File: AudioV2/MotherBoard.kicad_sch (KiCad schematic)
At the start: 47 parts, among them J201 +15/-15/A_GND out, J202 PD module in (1=GND 2=+12V), SW402 PWR SW, SW501 DEST L (PHONE/MUTE/LINE), SW502 DEST R (PHONE/MUTE/LINE), U201 REC10K-2415DAW/H2, U202 L7809CV +9V, U402 PT2314E, U403 BP5293-50 +5V

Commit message: AudioV2: DC-DC を REC20K-2415DZ へ差し替え、電源要求を「ソケットあたり」で記録した
## なぜ

この箱はオペアンプを差し替えて聴く箱で、入力ブロードキャスト＋出力のみ MUX なので
10個が常時通電する。つまり +15V の要求は「NE5532 ×10」ではなく「挿す石 ×10、常時」で、
レールの余裕は**1ソケットあたり何 mA 使えるか**に翻訳しないと目的と噛み合わない。

Audio/datasheets/opamps/ の一次資料（在庫石の Icc）:
  MUSES03  20 mA/socket（10 mA max ×2 の変換基板）← 在庫の最悪
  NE5532   16 mA（ICC total、VO=0 無負荷。typ 6 mA）
  OPA627×2 15 mA / LT1364 15 mA / OPA1656 9.2 mA/pkg max

1ソケットあたりに使える電流（固定側を保守側の 63 mA として）:

              計測系そのまま  LDO を +15V へ  +5V_D も +15V へ
  REC10K       27.0 mA        19.0 mA         9.4 mA
  REC20K       60.4 mA        52.4 mA        42.8 mA

REC10K では計測系を触らなくても 27 mA/socket しか出ない。MUSES03(20mA) は通るが
ディスクリート DIP-8 モジュールは入らず、計測系を +15V へ寄せると NE5532 の max
16 mA すら割る。「差し替えて遊ぶ」という目的に対して REC10K は最初から窮屈だった。

## 差し替え

独立した3つの理由が同じ結論に集まった:
  ① 上のソケットあたり予算
  ② Cout の宿題 — 実レール容量は +15V/-15V とも 259.8uF（sch_facts rails）で
     REC10K の Cout ±270uF の 96%。記録が使ってきた「102uF」は娘基板のバルクが
     入る前の古い値だった。REC20K は ±3000uF で 11 倍の余裕
  ③ 計測系の電源を +15V へ寄せる余地（U1604 = 非絶縁バック = 1.2kHz スパーの
     容疑者を設計から消せる。これ自体は未実施）

DS を突き合わせた結果（Recom_REC20K-Z_Rev3-2025.pdf p9 / REC10K-AW_Rev2-2025.pdf p9）:
入力 9-36V・ピン配置・パッド座標は同一で、**違うのは推奨穴だけ**（Ø1.0 -> Ø1.4）。

  ⚠ NOW.md は以前から「PCB の穴径は REC20K 互換（Ø1.4）」と書いていたが、
    フットプリント REC10K-AW_1in_THT は drill 1.0 のままで意図が実装されていなかった。
    REC20K の 1.4mm ピンは入らない。

Library:REC20K-Z_1in_THT を新設（穴 Ø1.4・パッド 2.2mm で環状部 0.4mm 維持）。
Ø1.4 なら REC10K（ピン径 0.6）も挿さるので、この1個で両方いける
= NOW.md の「REC10K は後から戻せる」が本当に成立する形になった。

  AudioV2.kicad_sym            REC20K-2415DZ を追加（REC10K とピン配置同一）
  legacy/PowerModule.kicad_sch U201 の lib_id/Value/Footprint/Datasheet/Description
                               ⚠ .kicad_sch は先頭に lib_symbols のキャッシュを持つので
                                 キャッシュと実体の2箇所を直す必要がある

## F201（入口 T1.6A）は据え置いたが、意味が変わった

12V 入力・効率 88% で:
  いまの想定（10×20mA + 固定 63mA）  7.9 W → 0.75 A  (T1.6A の 47%)
  計測系を +15V へ寄せたとき        10.5 W → 1.00 A  (62%)
  REC20K を使い切ったとき           20.0 W → 1.89 A  (118%)

つまり F201 が「REC20K の能力ではなく設計予算」を上限にしている。意図的なら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
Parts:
- U201: value REC10K-2415DAW/H2 -> REC20K-2415DZ; footprint Library:REC10K-AW_1in_THT -> Library:REC20K-Z_1in_THT; symbol AudioV2:REC10K-2415DAW -> AudioV2:REC20K-2415DZ; MPN REC10K-2415DAW/H2 -> REC20K-2415DZ
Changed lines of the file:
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@@
 	)
 	(symbol
-		(lib_id "AudioV2:REC10K-2415DAW")
+		(lib_id "AudioV2:REC20K-2415DZ")
 		(at 111.76 76.2 0)
 		(unit 1)
@@
 			)
 		)
-		(property "Value" "REC10K-2415DAW/H2"
+		(property "Value" "REC20K-2415DZ"
 			(at 111.76 76.2 0)
 			(show_name no)
@@
 			)
 		)
-		(property "Footprint" "Library:REC10K-AW_1in_THT"
+		(property "Footprint" "Library:REC20K-Z_1in_THT"
 			(at 113.03 72.39 0)
 			(hide yes)
@@
 			)
 		)
-		(property "Datasheet" "https://recom-power.com/pdf/Econoline/REC10K-AW.pdf"
+		(property "Datasheet" "AudioV2/datasheets/Recom_REC20K-Z_Rev3-2025.pdf"
 			(at 112.268 74.422 0)
 			(hide yes)
@@
 			)
 		)
-		(property "Description" "Recom REC10K-2415DAW/H2 isolated DC/DC, 9-36Vin, ±15V/±333mA (10W), 1.6kVDC iso, DIP 1in x 1in, Cout ±270uF/rail, pin3=CTRL open=ON"
+		(property "Description" "Recom REC20K-2415DZ isolated DC/DC, 9-36Vin, ±15V/±667mA (20W), eff 88% typ, DIP 1in x 1in, Cout ±3000uF/rail, pin3=CTRL open=ON。REC10K-2415DAW/H2（±333mA・Cout ±270uF）から 2026-09-07 に差し替えた。理由は独立に3つ: ①ソケット10個が常時通電なので ±333mA だと 1ソケットあたり 27mA しか使えず、在庫の MUSES03（20mA）で既に窮屈 ②実レール容量 259.8uF が Cout ±270uF の 96% ③計測系の電源を +15V へ寄せる余地。ピン配置は REC10K と同一で、推奨穴が Ø1.0 -> Ø1.4 になるのでフットプリントも替えた（Ø1.4 なら REC10K も挿さる）"
 			(at 111.76 76.2 0)
 			(hide yes)
@@
 			)
 		)
-		(property "MPN" "REC10K-2415DAW/H2"
+		(property "MPN" "REC20K-2415DZ"
 			(at 111.76 76.2 0)
 			(hide yes)

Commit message: AudioV2: レビュー指摘 3・4 を反映（OCP/容量の訂正、旧注釈10個の掃除、J_RAIL501 の Value）
レビューコメント（電源差し替えと U1604 削除の主経路は成立、残る4点は方針/文書/配線手順）
のうち、判断を要しない 3 と 4 を直した。1 と 2 は NOW.md に未判断として置いた。

## 3. DECISIONS の記述訂正（自分の誤り2件）

- U201 の OCP を「150% Io」と書いていたが、それは REC10K の値。
  REC20K-2415DZ は **225% of rated IOUT**（nom. VIN=48VDC、Recom_REC20K-Z_Rev3-2025.pdf）
- 「+15V/-15V とも 259.8µF」は差し替え時点の値。同日の U1604 削除で C1606/C1619
  （計 20.2µF）が中間レールから +15V に載り、いまは **+15V 280.0µF / -15V 259.8µF**。
  REC10K の Cout ±270µF に対して 96% → **103.7% で上限超え**。REC20K の理由②は
  差し替え後にさらに強まった

## 4. MeasureControl の旧注釈を掃除

26 個の text のうち 10 個が 2026-09-01 の再アノテーション前の designator のままだった。
うち3つは内容が現物と食い違っていた:

- [3][4] 電源系の注釈が **削除済みの U1604(MBC2596) の構成を今も説明**していた
  → ⑥-A 後の実配線（ADC の LDO は +15V 直結）に書き直し
- [11] GND の注釈が **NetTie の対応を現物と逆に**書いていた
  （旧「NT702=A_GND─ADC_GND / NT701=ADC_GND_IN─D_GND」→ 現物は NT1601 / NT1602）
  → NT1603 の新設と「3つを近接させる」も足した

残り7個は designator の置換のみ（回路図で1個ずつ対応を確定してから）:
  U704→U1607 U706→U1603 U707→U1606 U708→U1609 U709→U1605
  Y701→Y1601 D701→D1601 A701→A1601
  R717→R1620 R718→R1604 R719→R1611 R720→R1605
  C745→C1614（TPS3307 VDD） C740→C1633（XC8107 CIN） C739→C1631（XC8107 CL）
  NT701→NT1602 NT702→NT1601

同座標・同文の重複 2 組（[13][14] / [15][16]）を1つずつに。残る旧 designator は 0。

## J_RAIL501 の Value

「RAIL IN」→「AMP_SEL OUT」。実ネットは AMP_SEL_L / A_GND / AMP_SEL_R で、
娘基板がスロット直結になる前の名残だった。Description は前回直してある。
Value 変更なので PARTS.md を再生成した（BOM の行が変わる。netlist は変わらない）。

## 1・2 は NOW.md に未判断として置いた

1. ADC 枝の PPTC（旧 F1603）を戻すか — 既に記載あり
2. 計測側の電源端子 J1602/J1603 を残すか — **基板を分けるかの判断の下流**。
   分けないなら J1601 も含めて3個とも不要。分けるなら **J1603 のピン並びが J201 と逆**
   （J201=+15/GND/−15、J1603=−15/GND/+15。ピン番号どおりに繋ぐとレールが入れ替わる）。
   J1602 は F1601 が端子の外側に付いた行き止まりで、⑥-A 後は U1607 1個の 12V 入口

## 検証

  check_sexpr.py -q AudioV2   13 ファイル / 問題 0
  kicad-run.sh erc            11 件（変化なし）
  kicad-run.sh netlist        部品 370 個・重複 0・footprint 未設定 0（変化なし）
  sch_import --roundtrip      6/6 OK
  再生成の冪等性               バイト一致
  gen_parts_bom.py --check    OK

Co-Authored-By: Claude Fabl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
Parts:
- J_RAIL501: value RAIL IN -> AMP_SEL OUT
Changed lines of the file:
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@@
 			)
 		)
-		(property "Value" "RAIL IN"
+		(property "Value" "AMP_SEL OUT"
 			(at 36.83 160.02 0)
 			(show_name no)
@@
 			)
 		)
-		(property "Description" "選択された Amp 出力の取り出し端子。1=AMP_SEL_L / 2=A_GND / 3=AMP_SEL_R で、DEST スイッチ(SW501/SW502)の手前。Value の RAIL IN と旧記述の +12V/A_GND/-12V は、娘基板がスロット直結(J_PWR/J_ANA)になる前の名残で電源ではない。A_GND 極を持つ唯一の音声取り出し口。"
+		(property "Description" "選択された Amp 出力の取り出し端子。1=AMP_SEL_L / 2=A_GND / 3=AMP_SEL_R で、DEST スイッチ(SW501/SW502)の手前。旧 Value の RAIL IN と旧記述の +12V/A_GND/-12V は、娘基板がスロット直結(J_PWR/J_ANA)になる前の名残で電源ではない。A_GND 極を持つ唯一の音声取り出し口。"
 			(at -13.97 49.53 0)
 			(hide yes)

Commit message: AudioV2: HP バッファを移設し、PT2314E の DGND を A_GND へ寄せて I²C にレベルシフタを入れた
未実装のまま「確定」に留まっていた2件を回路図に入れ、注釈・BOM の腐りを直した。

- HP バッファ移設（2026-09-06 確定）: legacy/OutputStage に U501（DIP-8 ソケット、
  標準実装 OPA1652）+ R501/R502 10Ω + C501/C502 470µF NP + R503/R504 100k +
  C503-C506。RV501 ワイパー側のラベルを PHONE_BUF_L/R に改名し、PHONE_L/R は
  バッファ出力になった。J_HP501 / J_LINE501 を 01x03（L / A_GND / R）にして帰路を入れた
- DGND→A_GND ＋ I²C 境界（2026-09-07 確定）: U402.25 を A_GND へ。境界は BSS138 ×2 の
  双方向レベルシフタ（Q401/Q402、PT 側 R412/R413 10k → VCC_TONE）。P82B96 を使わない
  理由（Sx 側 VOL 0.8–1.0 V が PT2314E VIL 1.0 V / RP2350 VIL 0.8 V を食い切る）は
  DECISIONS の実装節に一次資料の数字で置いた
- MeasureControl の注釈: 上書きしてしまった Pico ピン配置ノートを復元（GP9=NC）、
  R1605 / 3.3k の旧記述を消し、U1611 Description を実値（約30k・−115.5 dB）に直した
- NT1603 を in_bom no に揃え、PARTS.md は 385（ネットリスト 389 − NetTie 4）
- DECISIONS: PPTC「戻さない」の理由を言い直し（1・2行目は判定材料にならない、
  3行目の条件は X7R 割れに限らない、U201 の OCP は 230 % max @ nom. VIN 24 V）、
  ヘッドルーム −0.4 dBFS は typ 基準で余裕の確定ではないと追記（7.5k 案を併記）、
  U1611 の 47Ω 省略に CL 100 pF の根拠を足した

検証: check_sexpr 0 / roundtrip 全 OK / 再生成は冪等（バイト一致）/ ERC 11 件（型・件数とも
変化なし）/ ネットリスト 389 個・重複 0・フットプリント未設定 0 / 母板で座標の偶然一致なし

Co-Authored-By: Claude Fable 5.1 <noreply@anthropic.com>
Claude-Session: https://claude.ai/code/session_01VCArLcCGbMGgxvWJ5HFJiY
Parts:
- added C501, C502: 470uF 25V NP, Capacitor_THT:CP_Radial_D10.0mm_P5.00mm, symbol Device:C
- added C503, C504: 10uF 25V X7R, Capacitor_SMD:C_1206_3216Metric_Pad1.33x1.80mm_HandSolder, symbol Device:C
- added C505, C506: 100nF, Capacitor_SMD:C_1206_3216Metric_Pad1.33x1.80mm_HandSolder, symbol Device:C
- added Q401, Q402: BSS138, Package_TO_SOT_SMD:SOT-23, symbol Transistor_FET:BSS138
- added R412, R413: 10k, Resistor_SMD:R_1206_3216Metric_Pad1.30x1.75mm_HandSolder, symbol Device:R
- added R501, R502: 10R, Resistor_SMD:R_1206_3216Metric_Pad1.30x1.75mm_HandSolder, symbol Device:R
- added R503, R504: 100k, Resistor_SMD:R_1206_3216Metric_Pad1.30x1.75mm_HandSolder, symbol Device:R
- added U501: OPA1652, Package_DIP:DIP-8_W7.62mm_Socket, symbol Amplifier_Operational:NE5532
- J_HP501: value to Audio HP Buffer -> HP OUT; footprint TerminalBlock_Phoenix:TerminalBlock_Phoenix_MKDS-1,5-2-5.08_1x02_P5.08mm_Horizontal -> TerminalBlock_Phoenix:TerminalBlock_Phoenix_MKDS-1,5-3-5.08_1x03_P5.08mm_Horizontal; symbol Connector:Screw_Terminal_01x02 -> Connector:Screw_Terminal_01x03
- J_LINE501: footprint TerminalBlock_Phoenix:TerminalBlock_Phoenix_MKDS-1,5-2-5.08_1x02_P5.08mm_Horizontal -> TerminalBlock_Phoenix:TerminalBlock_Phoenix_MKDS-1,5-3-5.08_1x03_P5.08mm_Horizontal; symbol Connector:Screw_Terminal_01x02 -> Connector:Screw_Terminal_01x03
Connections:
- net +15V: now also C503.1, C505.1, U501.8 (V+)
- net -15V: now also C504.2, C506.2, U501.4 (V-)
- net 3V3: now also Q401.1 (G), Q402.1 (G)
- net A_GND: now also J_HP501.2 (Pin_2), J_LINE501.2 (Pin_2), U402.25 (DGND), C503.2, C504.1, C505.2, C506.1, R503.2, R504.2
- net D_GND: no longer U402.25 (DGND)
- net I2C_SCL: now also Q402.2 (S); no longer U402.27 (CLK)
- net I2C_SDA: now also Q401.2 (S); no longer U402.26 (DATA)
- net LINE_R: now also J_LINE501.3 (Pin_3); no longer J_LINE501.2 (Pin_2)
- net PHONE_L: now also C501.2, R503.1; no longer RV501.2
- net PHONE_R: now also J_HP501.3 (Pin_3), C502.2, R504.1; no longer J_HP501.2 (Pin_2), RV501.5
- net VCC_TONE: now also R412.1, R413.1
- new net HP_OUT_L: R501.1, U501.1, U501.2 (-)
- new net HP_OUT_R: R502.1, U501.6 (-), U501.7
- new net HP_RC_L: C501.1, R501.2
- new net HP_RC_R: C502.1, R502.2
- new net I2C_SCL_9V: Q402.3 (D), R413.2, U402.27 (CLK)
- new net I2C_SDA_9V: Q401.3 (D), R412.2, U402.26 (DATA)
- new net PHONE_BUF_L: RV501.2, U501.3 (+)
- new net PHONE_BUF_R: RV501.5, U501.5 (+)
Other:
- note added: "HP バッファ（2026-09-08、v1 HeadphoneBufferModule を 5xx で移設）: RV501 ワイパー → PHONE_BUF_L/R → U501 ユニティ → 10Ω → 470µF NP → PHONE_L/R → J_HP501 / 親。100k はジャック側のブリード。U501 は DIP-8 ソケット、標準実装 OPA1652。LINE はバッファ無し（RV502 直出し）のまま。配線はピン先ラベル（このシートの流儀）。"
- note added: "I²C レベルシフタ（2026-09-08）: Pico 側 3V3 バス I2C_SDA/SCL（プルアップは MeasureControl の R1653/R1654 4.7k）↔ PT2314E 側 9V バス I2C_SDA_9V/SCL_9V（R412/R413 10k → VCC_TONE）。BSS138 ゲート=3V3。同時に U402 pin25 DGND をチップの足元で A_GND へ（旧 D_GND）。片方だけでは成立しない（DECISIONS「DGND はチップの足元で A_GND へ」）。"

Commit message: AudioV2: J1602 / J1603 のピン並びを母板の J202 / J201 に揃えた
計測側の電源端子が母板側と逆順だった（J1603: -15/GND/+15 vs J201: +15/A_GND/-15、
J1602: +12V/GND vs J202: GND/+12V）。配線・ラベル・F1601 は動かさず、シンボルを
左右ミラーしてピンの x を入れ替えた（J1602 はアンカーも 1 ピッチ移動）。
J201 の Value「+15/-15/A_GND out」を実ピン順「+15/A_GND/-15 out」に直した（素材 → 再生成）。
端子を残すか外すかは B5 のハーネス判断のまま。J1601（AUDIO、R/L 2P）は J_RAIL501（L/A_GND/R 3P）
と形が違う点を NOW に書いた。

検証: kicad-cli ネットリストで J1603 1=+15V 2=A_GND 3=-15V、J1602 1=PD_GND 2=F1601 側を確認。
ERC 11 件（変化なし）・部品 389・重複 0・check_sexpr 0・roundtrip OK・再生成バイト一致。

Co-Authored-By: Claude Fable 5.1 <noreply@anthropic.com>
Claude-Session: https://claude.ai/code/session_01VCArLcCGbMGgxvWJ5HFJiY
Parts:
- J201: value +15/-15/A_GND out -> +15/A_GND/-15 out
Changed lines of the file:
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@@
 			)
 		)
-		(property "Value" "+15/-15/A_GND out"
+		(property "Value" "+15/A_GND/-15 out"
 			(at 115.57 50.8 0)
 			(show_name no)

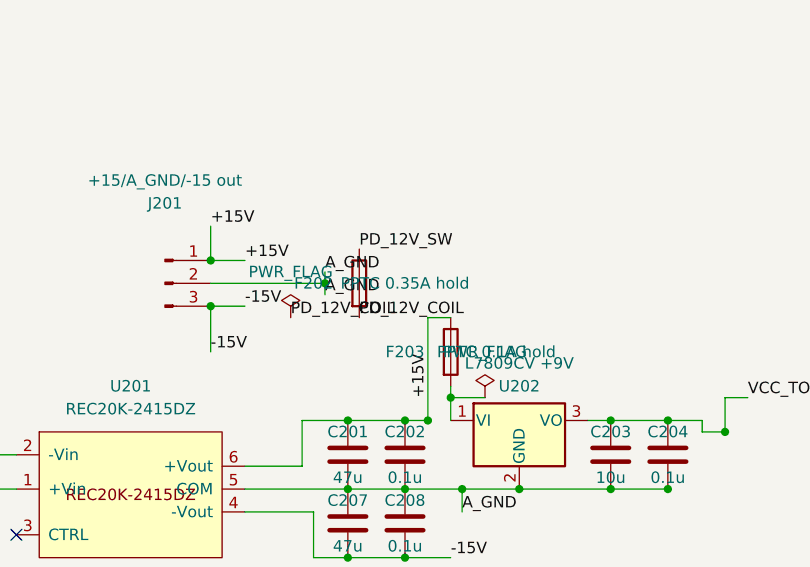
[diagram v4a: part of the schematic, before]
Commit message: AudioV2: ヒューズ / PPTC を入手性で型番決めし、5 個の FP を軸リードから実物に差し替えた
査読の指摘「F201 は Value 5×20 なのに FP が軸リード。他の 4 個も同じ」を潰した。

- 5×20 ガラス管（F201 T1.6A、F1601 T1A）: ホルダ Schurter OGN 0031.8201（DigiKey 在庫 6 万・¥240）。
  FP は KiCad 標準 Fuseholder_Cylinder-5x20mm_Schurter_0031_8201_Horizontal_Open
- PPTC（F202 / F203 / F1602）: Littelfuse RXEF040 / RXEF010 / RXEF050（在庫 2〜8 万）。
  Bourns MF-R040 / 010 / 050 も同寸で挿さる。F202 は 0.35 A の品が両社に無いので 0.40 A に寄せた
  （コイル枝のピークは約 0.16 A）。FP は Library:PPTC_Radial_D7.9mm_T3.1mm_P5.08mm を新設
  （DigiKey パラメータ: φ7.4〜7.9 × 3.0〜3.1、リード間隔 5.05 / 5.10。メーカー DS は 403 で未取得。
  穴 1.1 でピッチの差を吸収）
- 各 F の Description に型番と理由、PARTS.md の手書き行と NOW.md を更新

検証: 再生成バイト一致・check_sexpr 0（新 FP も）・kicad-cli fp export で FP 読込 OK・roundtrip OK・
ERC 11 件（変化なし）・部品 389・重複 0・フットプリント未設定 0

Co-Authored-By: Claude Fable 5.1 <noreply@anthropic.com>
Claude-Session: https://claude.ai/code/session_01VCArLcCGbMGgxvWJ5HFJiY
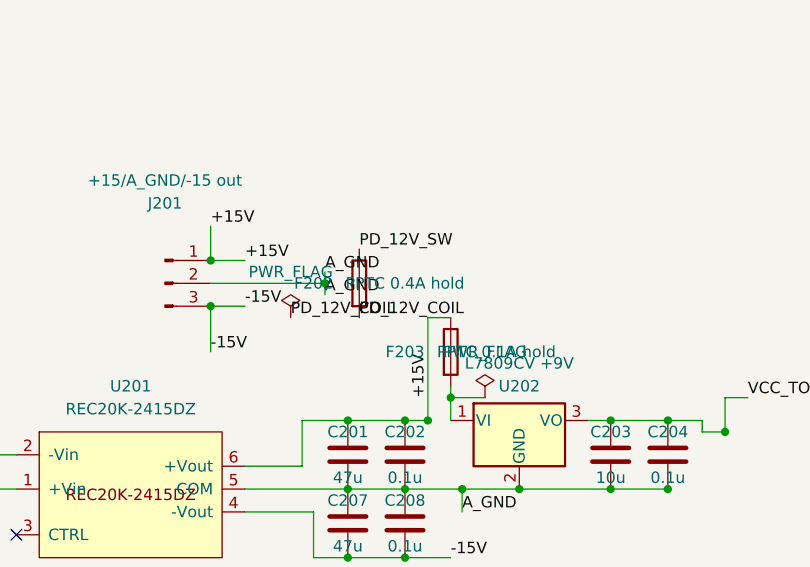
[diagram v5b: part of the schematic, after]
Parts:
- F201: footprint Resistor_THT:R_Axial_DIN0411_L9.9mm_D3.6mm_P12.70mm_Horizontal -> Fuse:Fuseholder_Cylinder-5x20mm_Schurter_0031_8201_Horizontal_Open
- F202: value PPTC 0.35A hold -> PPTC 0.4A hold; footprint Resistor_THT:R_Axial_DIN0411_L9.9mm_D3.6mm_P12.70mm_Horizontal -> Library:PPTC_Radial_D7.9mm_T3.1mm_P5.08mm
- F203: footprint Resistor_THT:R_Axial_DIN0411_L9.9mm_D3.6mm_P12.70mm_Horizontal -> Library:PPTC_Radial_D7.9mm_T3.1mm_P5.08mm
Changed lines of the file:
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@@
 			)
 		)
-		(property "Footprint" "Resistor_THT:R_Axial_DIN0411_L9.9mm_D3.6mm_P12.70mm_Horizontal"
+		(property "Footprint" "Fuse:Fuseholder_Cylinder-5x20mm_Schurter_0031_8201_Horizontal_Open"
 			(at -12.7 45.72 0)
 			(hide yes)
@@
 			)
 		)
-		(property "Description" ""
+		(property "Description" "入口ヒューズ（PD 12V → U201 REC20K）。ホルダは Schurter OGN 0031.8201（基板用 5×20 オープン型、DigiKey 在庫 6 万・¥240、KiCad 標準 FP）。中身は 5×20 ガラス管スローブロー T1.6A（例: Bel 0652C1000/1600-11、Littelfuse 0218 系、秋月の 5.2×20 スロー品も挿さる）。2026-09-09 に軸リード FP からホルダ FP へ直した"
 			(at -12.7 45.72 0)
 			(hide yes)
@@
 			)
 		)
-		(property "Value" "PPTC 0.35A hold"
+		(property "Value" "PPTC 0.4A hold"
 			(at 142.24 62.23 0)
 			(show_name no)
@@
 			)
 		)
-		(property "Footprint" "Resistor_THT:R_Axial_DIN0411_L9.9mm_D3.6mm_P12.70mm_Horizontal"
+		(property "Footprint" "Library:PPTC_Radial_D7.9mm_T3.1mm_P5.08mm"
 			(at -12.7 45.72 0)
 			(hide yes)
@@
 			)
 		)
-		(property "Description" ""
+		(property "Description" "リレーコイル電源（U403 前）の PPTC。0.35 A の品は Littelfuse/Bourns とも無いので 0.40 A に寄せた（コイル枝のピークは約 0.16 A）。ラジアル PPTC。Littelfuse RXEF040（Ih 0.40 A / It 0.80 A / 72 V）。Bourns MF-R040 も同寸で可。FP は DigiKey の寸法（φ7.4〜7.9×3.1、ピッチ 5.05〜5.10）から起こした Library の自作。2026-09-09 に軸リード FP から直した"
 			(at -12.7 45.72 0)
 			(hide yes)
@@
 			)
 		)
-		(property "Footprint" "Resistor_THT:R_Axial_DIN0411_L9.9mm_D3.6mm_P12.70mm_Horizontal"
+		(property "Footprint" "Library:PPTC_Radial_D7.9mm_T3.1mm_P5.08mm"
 			(at -12.7 45.72 0)
 			(hide yes)
@@
 			)
 		)
-		(property "Description" ""
+		(property "Description" "+9V LDO（U202）入口の PPTC。ラジアル PPTC。Littelfuse RXEF010（Ih 0.10 A / It 0.20 A / 60 V）。Bourns MF-R010 も同寸で可。FP は DigiKey の寸法（φ7.4〜7.9×3.1、ピッチ 5.05〜5.10）から起こした Library の自作。2026-09-09 に軸リード FP から直した"
 			(at -12.7 45.72 0)
 			(hide yes)
